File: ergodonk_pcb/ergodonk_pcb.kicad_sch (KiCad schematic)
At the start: 132 parts, among them J1 TRRS, J11 Pimaroni Trackball, Q1 TIP120, SW08_RH10 SW_PUSH_LED, SW1 SW_PUSH_LED, SW10 SW_PUSH_LED, SW11 SW_PUSH_LED, SW12 SW_PUSH_LED, SW13 SW_PUSH_LED, SW14 SW_PUSH_LED, SW15 SW_PUSH_LED, SW16 SW_PUSH_LED, SW17 SW_PUSH_LED, SW18_RH10 SW_PUSH_LED, SW2 SW_PUSH_LED, SW20 SW_PUSH_LED, SW21 SW_PUSH_LED, SW22 SW_PUSH_LED, SW23 SW_PUSH_LED, SW24 SW_PUSH_LED, SW25 SW_PUSH_LED, SW26 SW_PUSH_LED, SW27 SW_PUSH_LED, SW28_RH10 SW_PUSH_LED, SW3 SW_PUSH_LED, SW30 SW_PUSH_LED, SW31 SW_PUSH_LED, SW32 SW_PUSH_LED, SW33 SW_PUSH_LED, SW34 SW_PUSH_LED, SW35 SW_PUSH_LED, SW36 SW_PUSH_LED, SW37 SW_PUSH_LED, SW38_RH10 SW_PUSH_LED, SW4 SW_PUSH_LED, SW40 SW_PUSH_LED, SW42 SW_PUSH_LED, SW43 SW_PUSH_LED, SW44 SW_PUSH_LED, SW45 SW_PUSH_LED, SW46 SW_PUSH_LED, SW47 SW_PUSH_LED, SW48_RH10 SW_PUSH_LED, SW5 SW_PUSH_LED, SW50 SW_PUSH_LED, SW51 SW_PUSH_LED, SW52 SW_PUSH_LED, SW53 SW_PUSH_LED, SW54 SW_PUSH_LED, SW55 SW_PUSH_LED, SW56 SW_PUSH_LED, SW57 SW_PUSH_LED, SW58 SW_PUSH_LED, SW6 SW_PUSH_LED, SW7 SW_PUSH_LED, U10 Pico

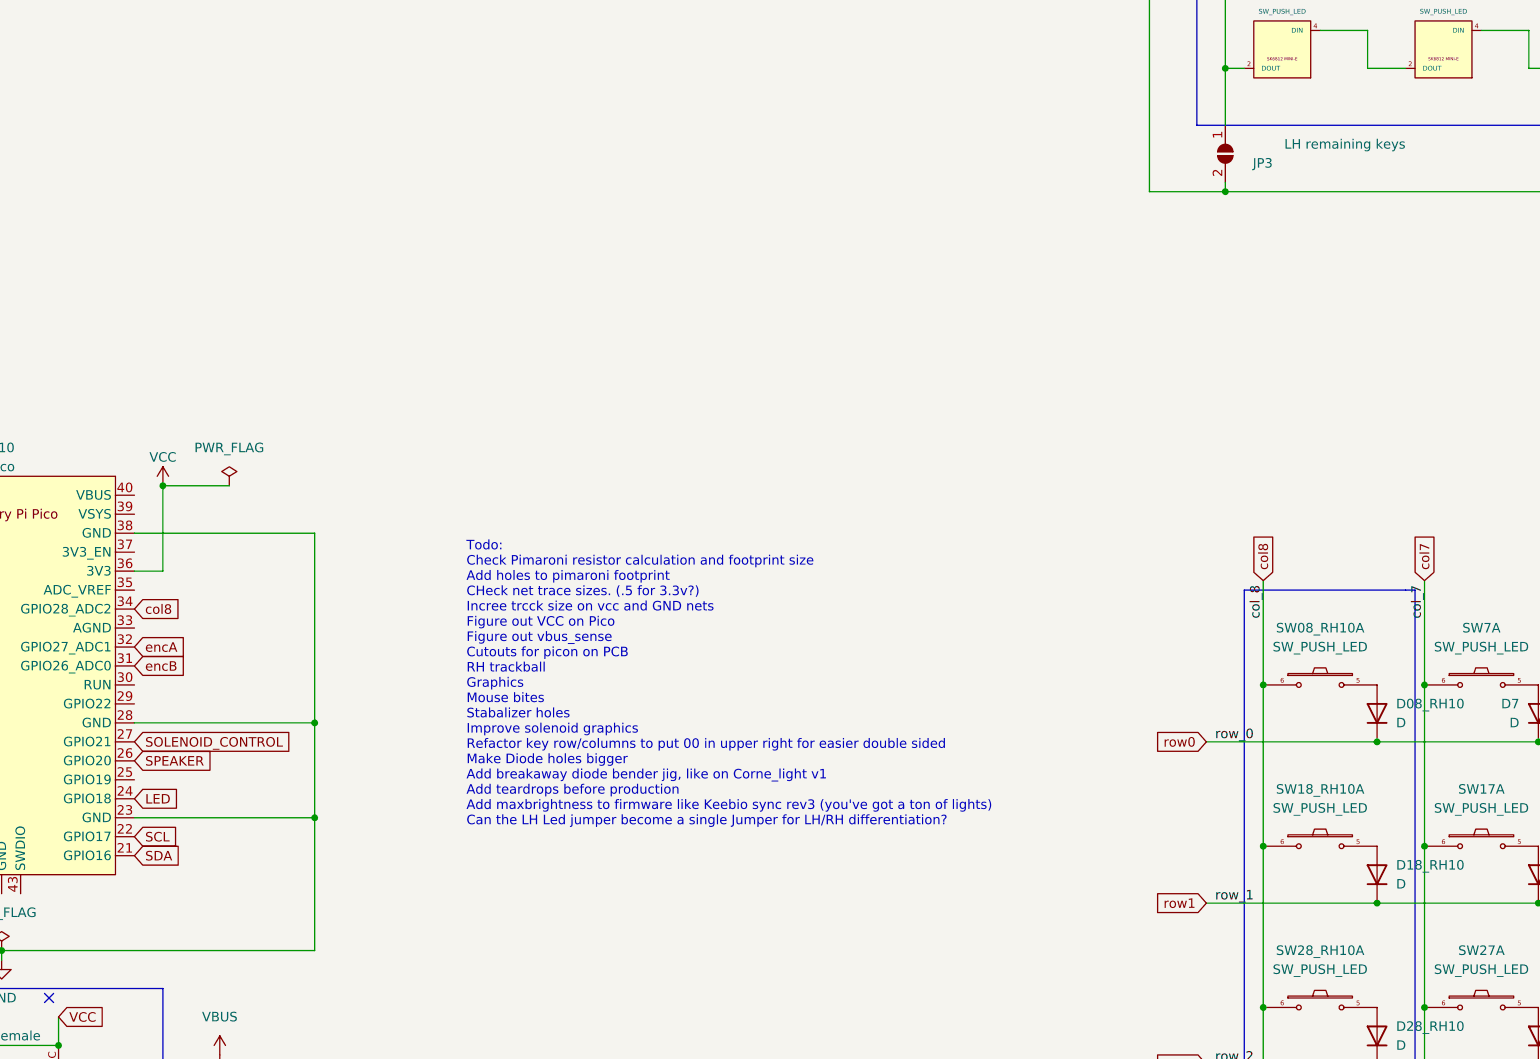
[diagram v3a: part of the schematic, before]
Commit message: Regenerated .dsn with ground and VCC zones
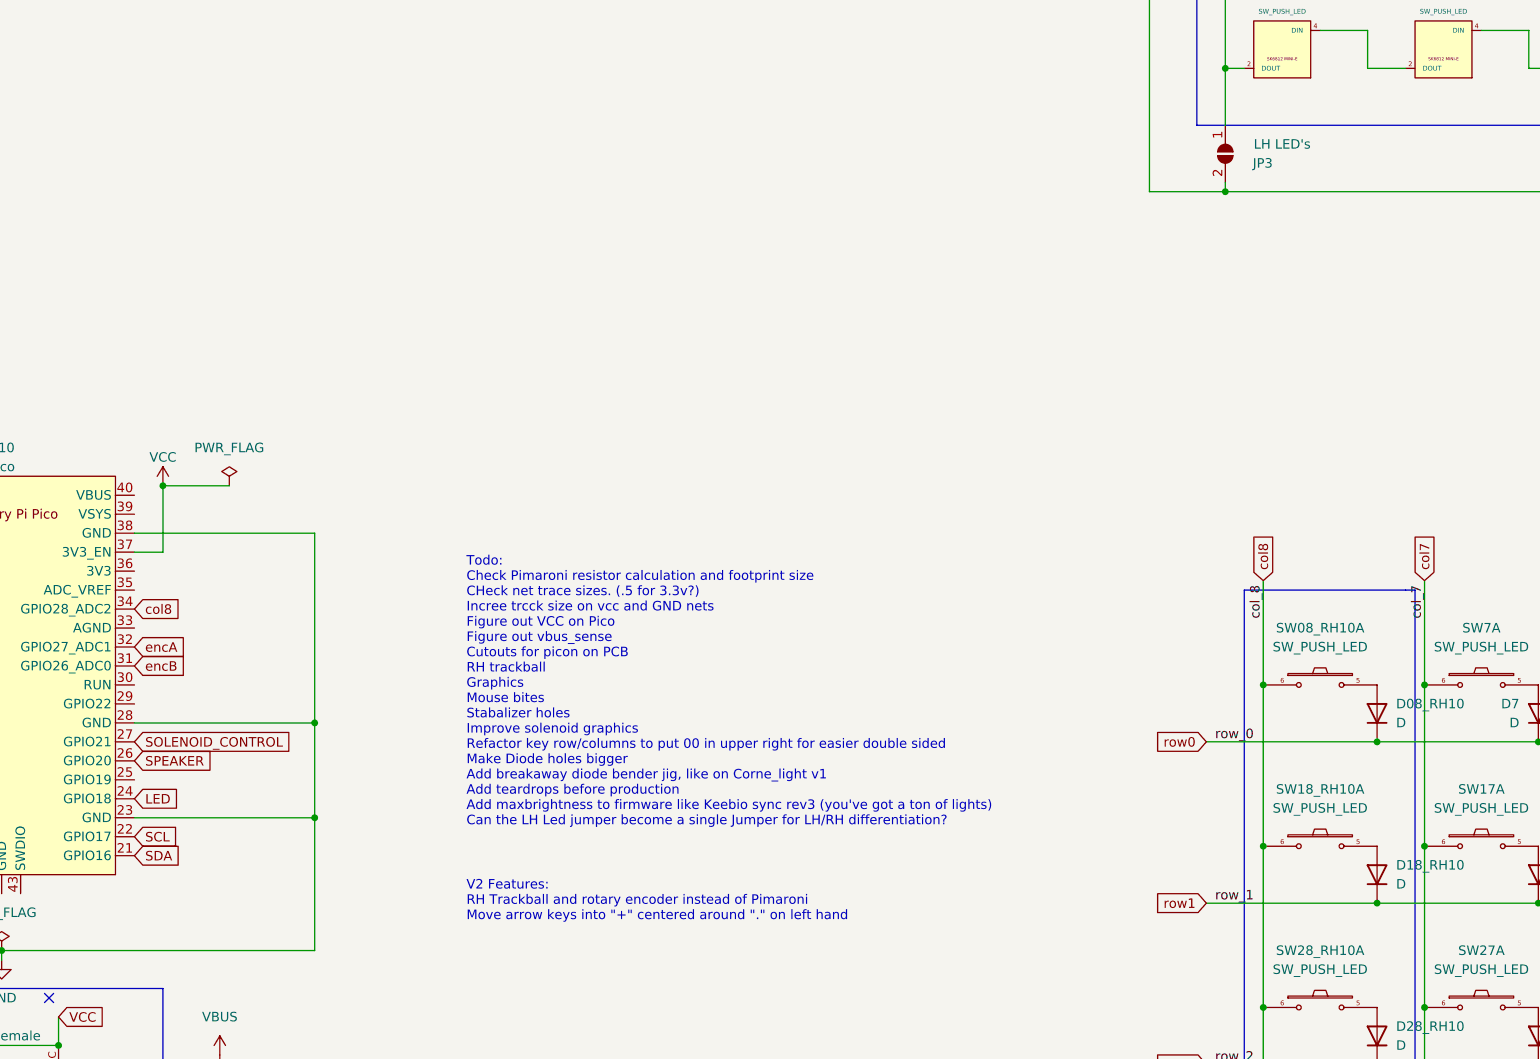
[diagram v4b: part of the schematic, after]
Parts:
- JP3: value LH remaining keys -> LH LED's
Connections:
- net VCC: now also U10.37 (3V3_EN); no longer U10.36 (3V3)
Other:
- note added: "Todo: Check Pimaroni resistor calculation and footprint size CHeck net trace sizes. (.5 for 3.3v?) Incree trcck size on vcc and GND nets Figure out VCC on Pico Figure out vbus_sense Cutouts for picon on PCB RH trackball Graphics Mouse bites Stabalizer holes Improve solenoid graphics Refactor key row/columns to put 00 in upper right for easier double sided Make Diode holes bigger Add breakaway dio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"
- note added: "V2 Features: RH Trackball and rotary encoder instead of Pimaroni Move arrow keys into "+" centered around "." on left hand"
- note removed: "Todo: Check Pimaroni resistor calculation and footprint size Add holes to pimaroni footprint CHeck net trace sizes. (.5 for 3.3v?) Incree trcck size on vcc and GND nets Figure out VCC on Pico Figure out vbus_sense Cutouts for picon on PCB RH trackball Graphics Mouse bites Stabalizer holes Improve solenoid graphics Refactor key row/columns to put 00 in upper right for easier double sided Make Diod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"
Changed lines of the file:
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@@
     (stroke (width 0) (type default))
   )
-  (wire (pts (xy 66.04 19.05) (xy 66.04 30.48))
+  (wire (pts (xy 66.04 19.05) (xy 66.04 27.94))
     (stroke (width 0) (type default))
   )
@@
     (stroke (width 0) (type default))
   )
-  (wire (pts (xy 62.23 30.48) (xy 66.04 30.48))
-    (stroke (width 0) (type default))
-  )
   (wire (pts (xy 256.54 110.49) (xy 256.54 132.08))
     (stroke (width 0) (type default))
@@
     (stroke (width 0) (type default))
   )
+  (wire (pts (xy 62.23 27.94) (xy 66.04 27.94))
+    (stroke (width 0) (type default))
+  )
   (wire (pts (xy 356.87 -87.63) (xy 350.52 -87.63))
     (stroke (width 0) (type default))
@@
     (effects (font (size 1.27 1.27)) (justify left bottom))
   )
-  (text "Todo:\nCheck Pimaroni resistor calculation and footprint size\nAdd holes to pimaroni footprint\nCHeck net trace sizes. (.5 for 3.3v?)\nIncree trcck size on vcc and GND nets\nFigure out VCC on Pico\nFigure out vbus_sense\nCutouts for picon on PCB\nRH trackball\nGraphics\nMouse bites\nStabalizer holes\nImprove solenoid graphics\nRefactor key row/columns to put 00 in upper right for easier double sided\nMake Diode holes bigger\nAdd breakaway diode bender jig, like on Corne_light v1\nAdd teardrops before production\nAdd maxbrightness to firmware like Keebio sync rev3 (you've got a ton of lights)\nCan the LH Led jumper become a single Jumper for LH/RH differentiation?"
+  (text "Todo:\nCheck Pimaroni resistor calculation and footprint size\nCHeck net trace sizes. (.5 for 3.3v?)\nIncree trcck size on vcc and GND nets\nFigure out VCC on Pico\nFigure out vbus_sense\nCutouts for picon on PCB\nRH trackball\nGraphics\nMouse bites\nStabalizer holes\nImprove solenoid graphics\nRefactor key row/columns to put 00 in upper right for easier double sided\nMake Diode holes bigger\nAdd breakaway diode bender jig, like on Corne_light v1\nAdd teardrops before production\nAdd maxbrightness to firmware like Keebio sync rev3 (you've got a ton of lights)\nCan the LH Led jumper become a single Jumper for LH/RH differentiation?"
     (at 106.68 64.77 0)
     (effects (font (size 1.27 1.27)) (justify left bottom))
@@
     (effects (font (size 1.27 1.27)) (justify left bottom))
   )
+  (text "V2 Features:\nRH Trackball and rotary encoder instead of Pimaroni\nMove arrow keys into \"+\" centered around \".\" on left hand"
+    (at 106.68 77.47 0)
+    (effects (font (size 1.27 1.27)) (justify left bottom))
+  )
   (text "F keys" (at 229.87 -158.75 0)
     (effects (font (size 1.27 1.27)) (justify left bottom))
@@
       (effects (font (size 1.27 1.27)) (justify left))
     )
-    (property "Value" "LH remaining keys" (at 232.41 -26.67 90)
+    (property "Value" "LH LED's" (at 219.71 -26.67 90)
       (effects (font (size 1.27 1.27)) (justify left))
     )

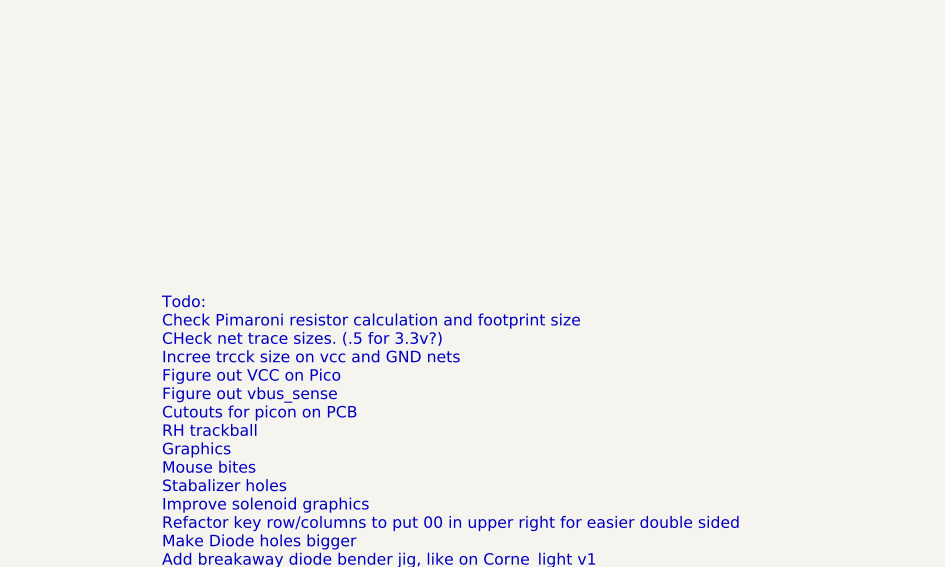
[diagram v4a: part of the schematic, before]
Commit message: Revised solenoid footrpints and layout for easier soldering and better fit
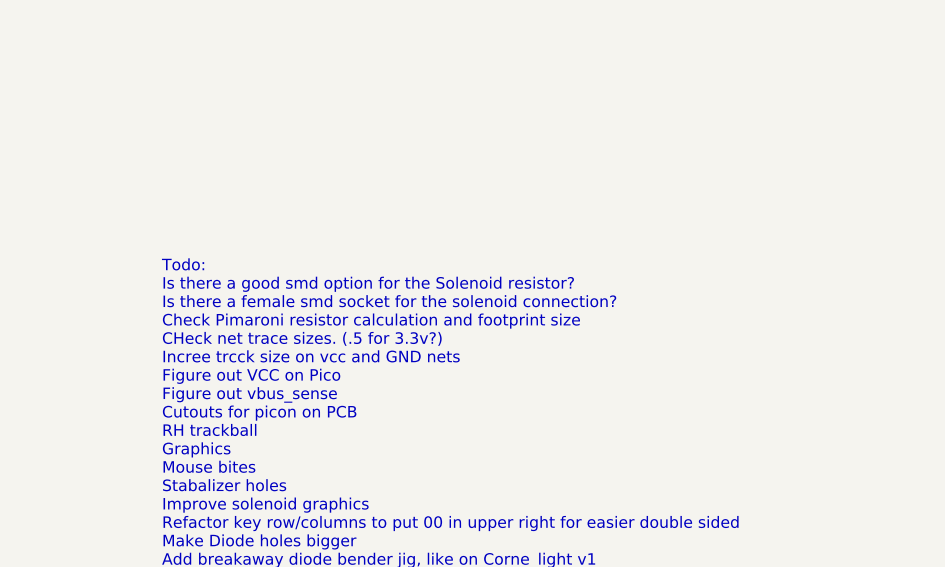
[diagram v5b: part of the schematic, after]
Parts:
- D_SOL_1: footprint ergodonk_kicad_library:MUR340S_IN4004_TH -> ergodonk_kicad_library:MUR340S_IN4001_TH
- R2: footprint Resistor_THT:R_Axial_DIN0207_L6.3mm_D2.5mm_P10.16mm_Horizontal -> Resistor_THT:R_Axial_DIN0309_L9.0mm_D3.2mm_P12.70mm_Horizontal
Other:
- note added: "Todo: Is there a good smd option for the Solenoid resistor? Is there a female smd socket for the solenoid connection? Check Pimaroni resistor calculation and footprint size CHeck net trace sizes. (.5 for 3.3v?) Incree trcck size on vcc and GND nets Figure out VCC on Pico Figure out vbus_sense Cutouts for picon on PCB RH trackball Graphics Mouse bites Stabalizer holes Improve solenoid graphics Ref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"
- note removed: "Todo: Check Pimaroni resistor calculation and footprint size CHeck net trace sizes. (.5 for 3.3v?) Incree trcck size on vcc and GND nets Figure out VCC on Pico Figure out vbus_sense Cutouts for picon on PCB RH trackball Graphics Mouse bites Stabalizer holes Improve solenoid graphics Refactor key row/columns to put 00 in upper right for easier double sided Make Diode holes bigger Add breakaway dio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"
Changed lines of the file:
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@@
     (effects (font (size 1.27 1.27)) (justify left bottom))
   )
-  (text "Todo:\nCheck Pimaroni resistor calculation and footprint size\nCHeck net trace sizes. (.5 for 3.3v?)\nIncree trcck size on vcc and GND nets\nFigure out VCC on Pico\nFigure out vbus_sense\nCutouts for picon on PCB\nRH trackball\nGraphics\nMouse bites\nStabalizer holes\nImprove solenoid graphics\nRefactor key row/columns to put 00 in upper right for easier double sided\nMake Diode holes bigger\nAdd breakaway diode bender jig, like on Corne_light v1\nAdd teardrops before production\nAdd maxbrightness to firmware like Keebio sync rev3 (you've got a ton of lights)\nCan the LH Led jumper become a single Jumper for LH/RH differentiation?"
+  (text "Todo:\nIs there a good smd option for the Solenoid resistor?\nIs there a female smd socket for the solenoid connection?\nCheck Pimaroni resistor calculation and footprint size\nCHeck net trace sizes. (.5 for 3.3v?)\nIncree trcck size on vcc and GND nets\nFigure out VCC on Pico\nFigure out vbus_sense\nCutouts for picon on PCB\nRH trackball\nGraphics\nMouse bites\nStabalizer holes\nImprove solenoid graphics\nRefactor key row/columns to put 00 in upper right for easier double sided\nMake Diode holes bigger\nAdd breakaway diode bender jig, like on Corne_light v1\nAdd teardrops before production\nAdd maxbrightness to firmware like Keebio sync rev3 (you've got a ton of lights)\nCan the LH Led jumper become a single Jumper for LH/RH differentiation?"
     (at 106.68 64.77 0)
     (effects (font (size 1.27 1.27)) (justify left bottom))
@@
       (effects (font (size 1.27 1.27)))
     )
-    (property "Footprint" "Resistor_THT:R_Axial_DIN0207_L6.3mm_D2.5mm_P10.16mm_Horizontal" (at 39.37 109.22 0)
+    (property "Footprint" "Resistor_THT:R_Axial_DIN0309_L9.0mm_D3.2mm_P12.70mm_Horizontal" (at 39.37 109.22 0)
       (effects (font (size 1.27 1.27)) hide)
     )
@@
       (effects (font (size 1.27 1.27)) (justify right))
     )
-    (property "Footprint" "ergodonk_kicad_library:MUR340S_IN4004_TH" (at 52.07 99.06 0)
+    (property "Footprint" "ergodonk_kicad_library:MUR340S_IN4001_TH" (at 52.07 99.06 0)
       (effects (font (size 1.27 1.27)) (justify bottom) hide)
     )

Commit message: Schematic cleanup for review/assistance
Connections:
- no-connect marks 4 -> 11
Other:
- note added: "??? Power???"
- note added: "Speaker"
- note added: "Todo: Thumb cluster detach? Is there a good smd option for the Solenoid resistor? Is there a female smd socket for the solenoid connection? Check Pimaroni resistor calculation and footprint size CHeck net trace sizes. (.5 for 3.3v?) Incree trcck size on vcc and GND nets Figure out VCC on Pico Figure out vbus_sense Cutouts for picon on PCB RH trackball Graphics Mouse bites Stabalizer holes Improve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"
- note removed: "Speaker! (WTF not!)"
- note removed: "Todo: Is there a good smd option for the Solenoid resistor? Is there a female smd socket for the solenoid connection? Check Pimaroni resistor calculation and footprint size CHeck net trace sizes. (.5 for 3.3v?) Incree trcck size on vcc and GND nets Figure out VCC on Pico Figure out vbus_sense Cutouts for picon on PCB RH trackball Graphics Mouse bites Stabalizer holes Improve solenoid graphics Ref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"
- moved on the sheet: D08_RH10, D1, D10, D11, D12, D13, D14, D15, D16, D17, D18_RH10, D2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
